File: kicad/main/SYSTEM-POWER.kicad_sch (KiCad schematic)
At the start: 93 parts, among them Q1 AO4407C, Q13 AO4407C, Q16 AO3401, Q17 AO3401, Q19 AO3400, Q23 AO3400, U12 XRNR4030-10UH_M, U16 HT7533-1_C14289, U21 AP64501SP-13, U22 AP64501SP-13, U24 AP64501SP-13, U5 MT3608

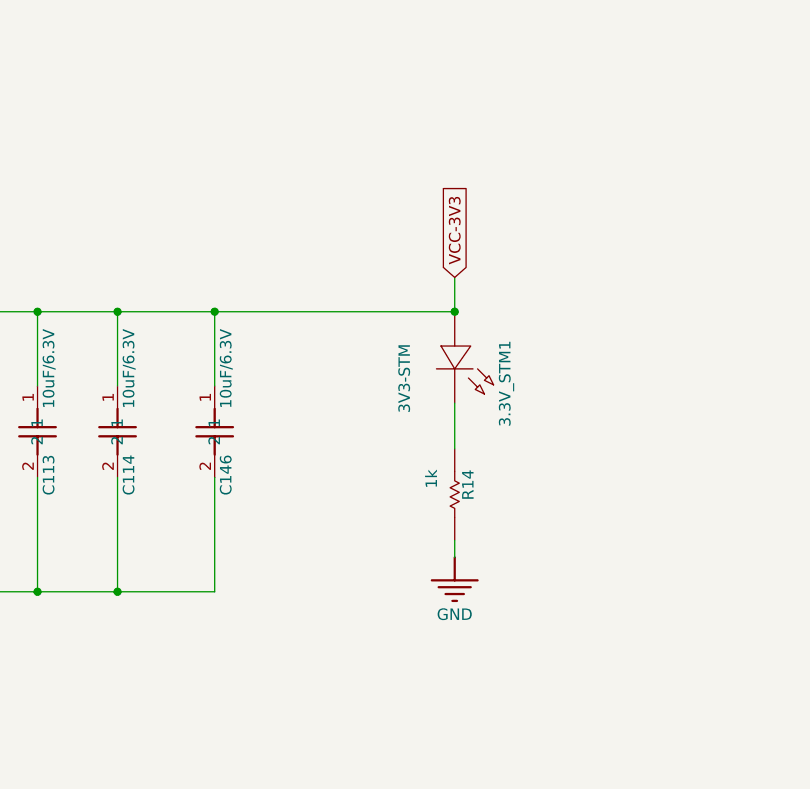
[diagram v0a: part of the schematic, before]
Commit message: Assigned footprints
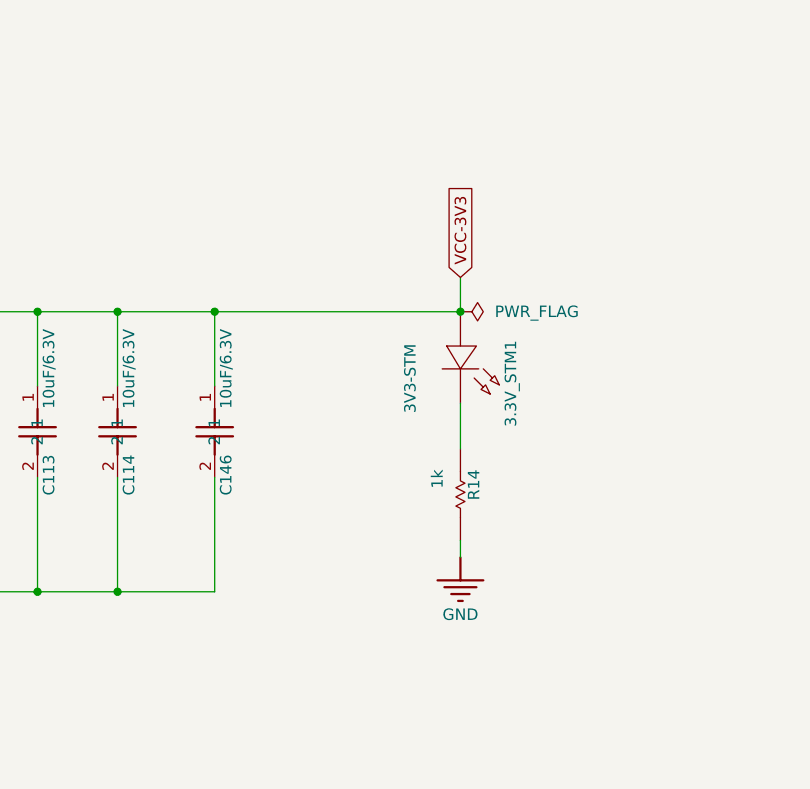
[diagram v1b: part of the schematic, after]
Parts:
- C14, C22: footprint (none) -> Capacitor_SMD:C_0603_1608Metric
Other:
- moved on the sheet: 3.3V_STM1, R14
